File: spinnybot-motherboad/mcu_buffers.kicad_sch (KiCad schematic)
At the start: 13 parts, among them Q3 BC846, U2 XBP9B-DMWTB002, U5 ESP32-DEVKITC-32D, U7 SN74AHCT541DW

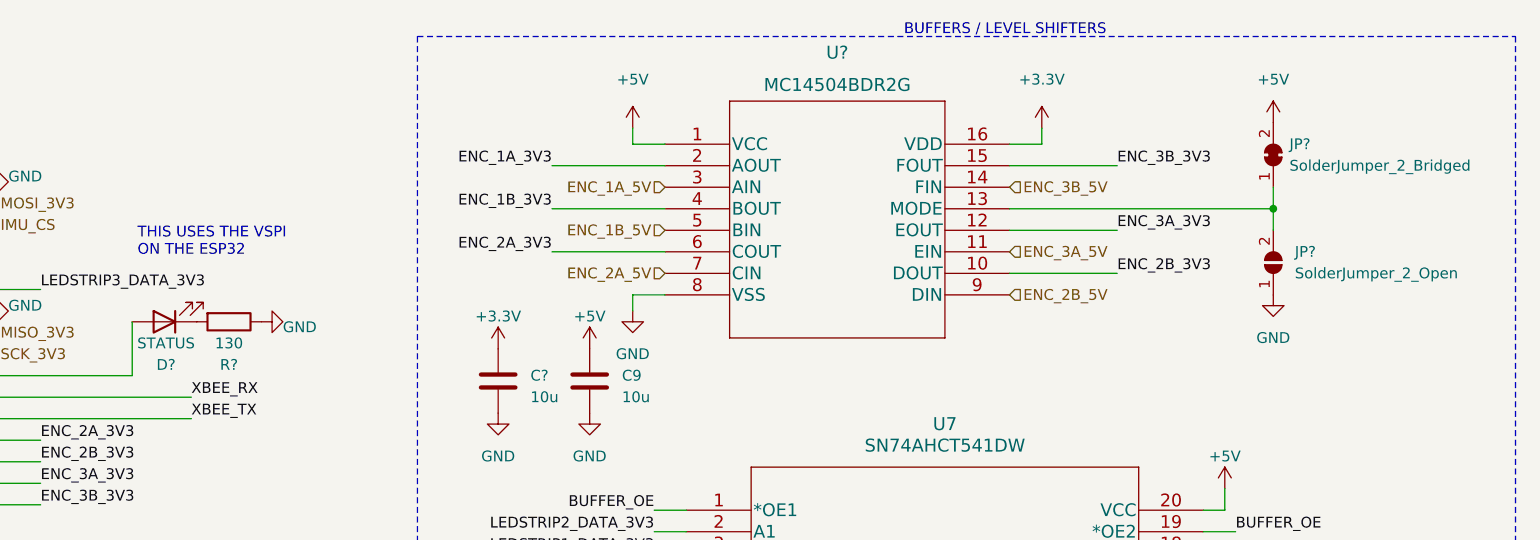
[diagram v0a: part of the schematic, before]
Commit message: Added 4 pin JST connector footprint and assigned footprints
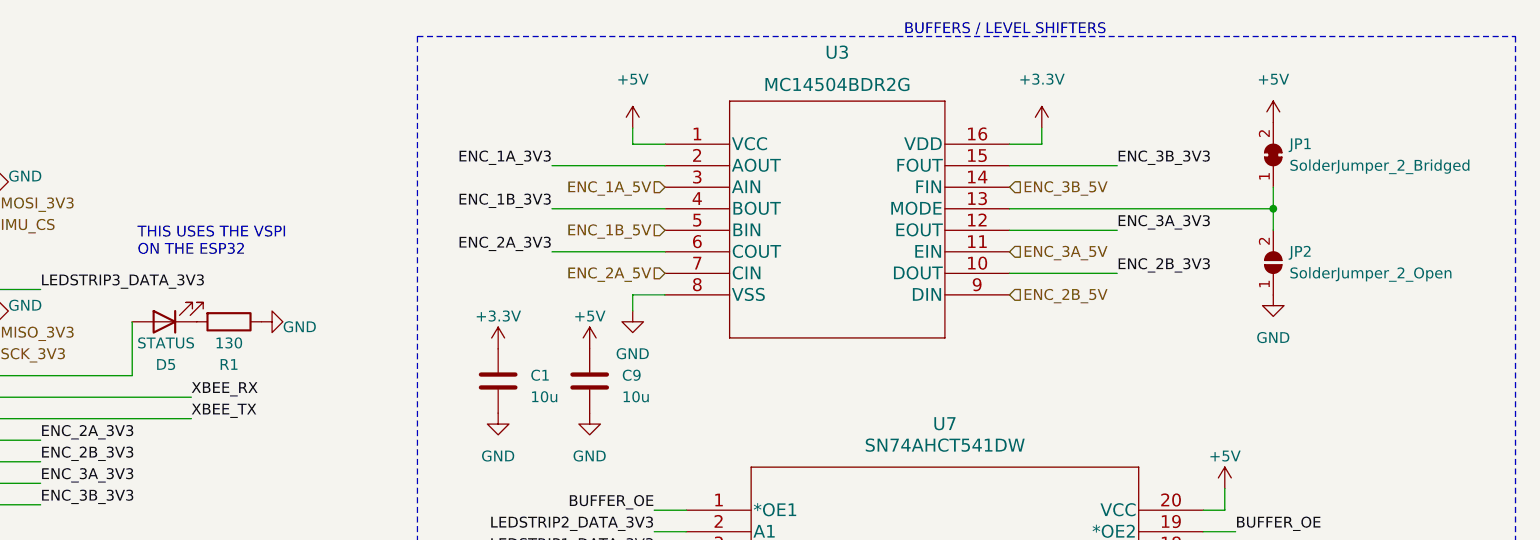
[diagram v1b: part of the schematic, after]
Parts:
- JP1: renamed from JP?; footprint (none) -> Jumper:SolderJumper-2_P1.3mm_Bridged_Pad1.0x1.5mm
- JP2: renamed from JP?; footprint (none) -> Jumper:SolderJumper-2_P1.3mm_Open_Pad1.0x1.5mm
- gave numbers to parts that had none: 4
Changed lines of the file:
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@@
   (symbol (lib_id "MC14504BDR2G:MC14504BDR2G") (at 181.61 30.48 0) (unit 1)
     (in_bom yes) (on_board yes) (fields_autoplaced)
-    (property "Reference" "U?" (id 0) (at 201.93 19.685 0)
+    (property "Reference" "U3" (id 0) (at 201.93 19.685 0)
       (effects (font (size 1.524 1.524)))
     )
@@
   (symbol (lib_id "Device:C") (at 161.925 58.42 0) (unit 1)
     (in_bom yes) (on_board yes) (fields_autoplaced)
-    (property "Reference" "C?" (id 0) (at 165.735 57.7849 0)
+    (property "Reference" "C1" (id 0) (at 165.735 57.7849 0)
       (effects (font (size 1.27 1.27)) (justify left))
     )
@@
   (symbol (lib_id "Jumper:SolderJumper_2_Bridged") (at 253.365 31.75 90) (unit 1)
     (in_bom yes) (on_board yes) (fields_autoplaced)
-    (property "Reference" "JP?" (id 0) (at 255.27 30.4799 90)
+    (property "Reference" "JP1" (id 0) (at 255.27 30.4799 90)
       (effects (font (size 1.27 1.27)) (justify right))
     )
@@
       (effects (font (size 1.27 1.27)) (justify right))
     )
-    (property "Footprint" "" (id 2) (at 253.365 31.75 0)
+    (property "Footprint" "Jumper:SolderJumper-2_P1.3mm_Bridged_Pad1.0x1.5mm" (id 2) (at 253.365 31.75 0)
       (effects (font (size 1.27 1.27)) hide)
     )
@@
   (symbol (lib_id "Device:R") (at 130.175 51.435 270) (unit 1)
     (in_bom yes) (on_board yes) (fields_autoplaced)
-    (property "Reference" "R?" (id 0) (at 130.175 56.515 90))
+    (property "Reference" "R1" (id 0) (at 130.175 56.515 90))
     (property "Value" "130" (id 1) (at 130.175 53.975 90))
     (property "Footprint" "Resistor_SMD:R_0805_2012Metric_Pad1.20x1.40mm_HandSolder" (id 2) (at 130.175 49.657 90)
@@
   (symbol (lib_id "Jumper:SolderJumper_2_Open") (at 253.365 44.45 90) (unit 1)
     (in_bom yes) (on_board yes) (fields_autoplaced)
-    (property "Reference" "JP?" (id 0) (at 255.905 43.1799 90)
-      (effects (font (size 1.27 1.27)) (justify right))
-    )
-    (property "Value" "SolderJumper_2_Open" (id 1) (at 255.905 45.7199 90)
-      (effects (font (size 1.27 1.27)) (justify right))
-    )
-    (property "Footprint" "" (id 2) (at 253.365 44.45 0)
+    (property "Reference" "JP2" (id 0) (at 255.27 43.1799 90)
+      (effects (font (size 1.27 1.27)) (justify right))
+    )
+    (property "Value" "SolderJumper_2_Open" (id 1) (at 255.27 45.7199 90)
+      (effects (font (size 1.27 1.27)) (justify right))
+    )
+    (property "Footprint" "Jumper:SolderJumper-2_P1.3mm_Open_Pad1.0x1.5mm" (id 2) (at 253.365 44.45 0)
       (effects (font (size 1.27 1.27)) hide)
     )
@@
   (symbol (lib_id "Device:LED") (at 122.555 51.435 180) (unit 1)
     (in_bom yes) (on_board yes) (fields_autoplaced)
-    (property "Reference" "D?" (id 0) (at 122.7455 56.515 0))
+    (property "Reference" "D5" (id 0) (at 122.7455 56.515 0))
     (property "Value" "STATUS" (id 1) (at 122.7455 53.975 0))
     (property "Footprint" "LED_SMD:LED_0805_2012Metric_Pad1.15x1.40mm_HandSolder" (id 2) (at 122.555 51.435 0)

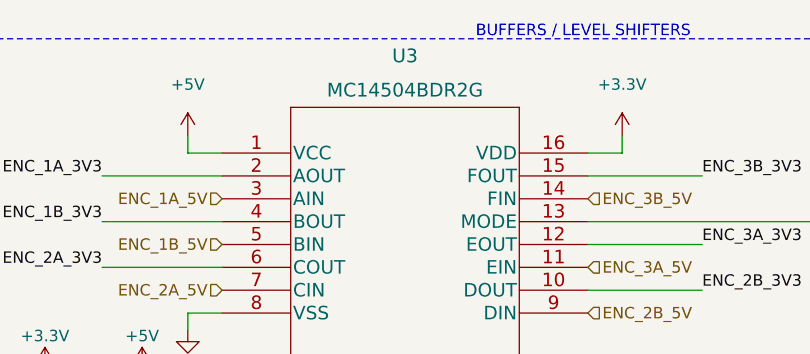
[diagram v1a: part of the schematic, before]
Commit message: Continued adding to board layout, added missing ESC connector footprint
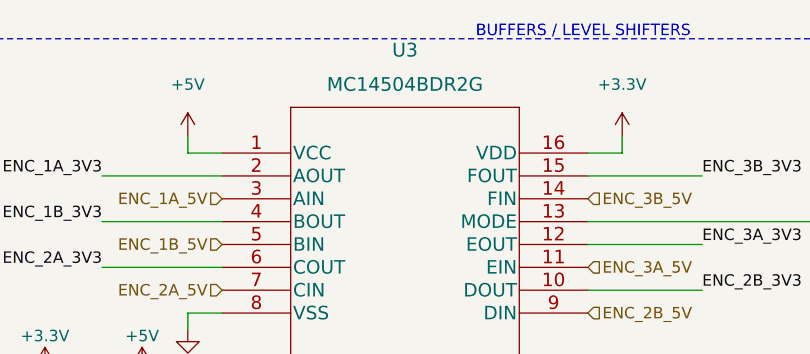
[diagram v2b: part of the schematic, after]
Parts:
- U3: footprint SOIC-16_ONS -> MC14504BDR2G:MC14504BDR2G
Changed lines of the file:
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@@
   (symbol (lib_id "MC14504BDR2G:MC14504BDR2G") (at 181.61 30.48 0) (unit 1)
     (in_bom yes) (on_board yes) (fields_autoplaced)
-    (property "Reference" "U3" (id 0) (at 201.93 19.685 0)
+    (property "Reference" "U3" (id 0) (at 201.93 19.05 0)
       (effects (font (size 1.524 1.524)))
     )
-    (property "Value" "MC14504BDR2G" (id 1) (at 201.93 23.495 0)
+    (property "Value" "MC14504BDR2G" (id 1) (at 201.93 22.86 0)
       (effects (font (size 1.524 1.524)))
     )
-    (property "Footprint" "SOIC-16_ONS" (id 2) (at 201.93 24.384 0)
+    (property "Footprint" "MC14504BDR2G:MC14504BDR2G" (id 2) (at 201.93 24.384 0)
       (effects (font (size 1.524 1.524)) hide)
     )

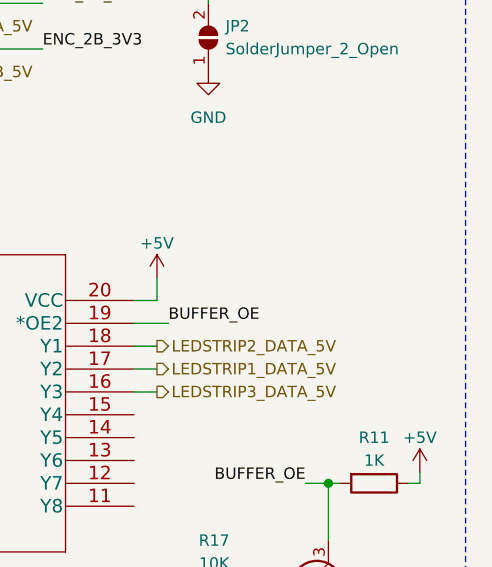
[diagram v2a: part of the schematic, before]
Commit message: Addressed Pratik's concerns about cap placement and missing caps
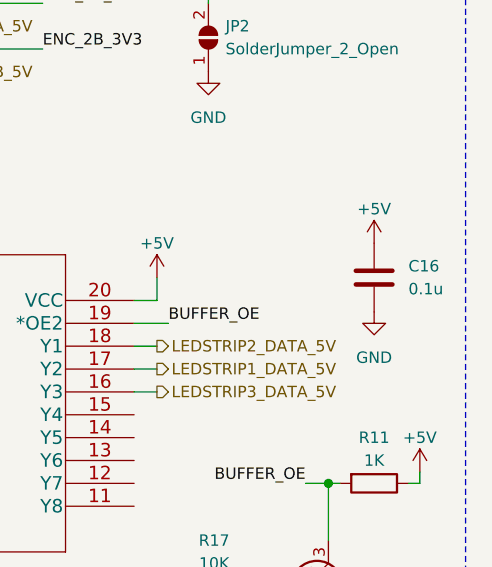
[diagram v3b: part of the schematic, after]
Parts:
- added C16: 0.1u, Capacitor_SMD:C_1206_3216Metric_Pad1.33x1.80mm_HandSolder, symbol Device:C
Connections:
- net +5V: now also C16.1
- net GND: now also C16.2
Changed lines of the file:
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@@
+    (pin "1")
+  )
+  (symbol (lib_id "power:+5V") (at 271.78 67.31 0) (unit 1)
+    (in_bom yes) (on_board yes) (fields_autoplaced)
+    (property "Reference" "#PWR0160" (id 0) (at 273.05 66.04 0)
+      (effects (font (size 1.27 1.27)) hide)
+    )
+    (property "Value" "+5V" (id 1) (at 271.78 63.5 0))
+    (property "Footprint" "" (id 2) (at 271.78 67.31 0)
+      (effects (font (size 1.27 1.27)) hide)
+    )
+    (property "Datasheet" "" (id 3) (at 271.78 67.31 0)
+      (effects (font (size 1.27 1.27)) hide)
+    )
     (pin "1")
   )
@@
     )
     (property "Datasheet" "" (id 3) (at 59.69 67.945 0)
+      (effects (font (size 1.27 1.27)) hide)
+    )
+    (pin "1")
+  )
+  (symbol (lib_id "power:GND") (at 271.78 74.93 0) (unit 1)
+    (in_bom yes) (on_board yes) (fields_autoplaced)
+    (property "Reference" "#PWR0161" (id 0) (at 273.05 73.66 0)
+      (effects (font (size 1.27 1.27)) hide)
+    )
+    (property "Value" "GND" (id 1) (at 271.78 80.01 0))
+    (property "Footprint" "" (id 2) (at 271.78 74.93 0)
+      (effects (font (size 1.27 1.27)) hide)
+    )
+    (property "Datasheet" "" (id 3) (at 271.78 74.93 0)
       (effects (font (size 1.27 1.27)) hide)
     )
@@
       (effects (font (size 1.27 1.27)) hide)
     )
+    (pin "1")
+    (pin "2")
+  )
+  (symbol (lib_id "Device:C") (at 271.78 71.12 0) (unit 1)
+    (in_bom yes) (on_board yes) (fields_autoplaced)
+    (property "Reference" "C16" (id 0) (at 275.59 69.8499 0)
+      (effects (font (size 1.27 1.27)) (justify left))
+    )
+    (property "Value" "0.1u" (id 1) (at 275.59 72.3899 0)
+      (effects (font (size 1.27 1.27)) (justify left))
+    )
+    (property "Footprint" "Capacitor_SMD:C_1206_3216Metric_Pad1.33x1.80mm_HandSolder" (id 2) (at 272.7452 74.93 0)
+      (effects (font (size 1.27 1.27)) hide)
+    )
+    (property "Datasheet" "~" (id 3) (at 271.78 71.12 0)
+      (effects (font (size 1.27 1.27)) hide)
+    )

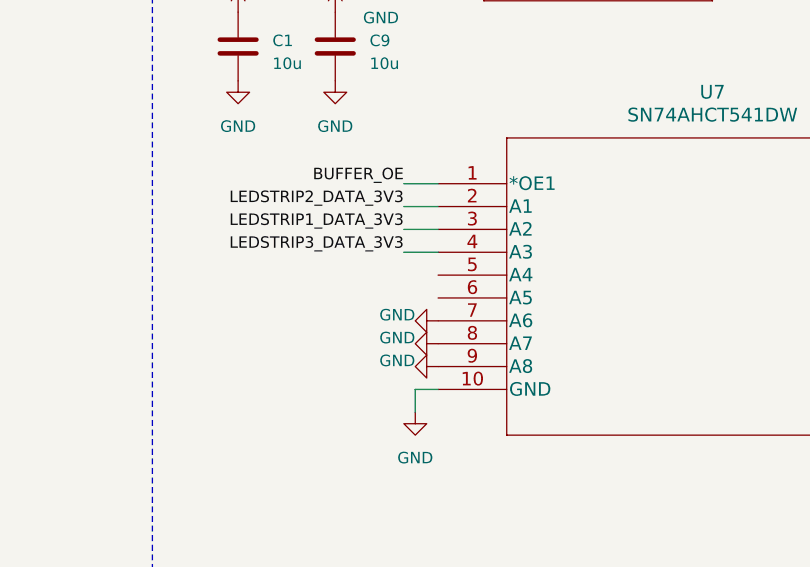
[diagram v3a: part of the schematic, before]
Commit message: tweaks to routing to make the ground plane more connected, add a top copper ground pour. move ESC FET.
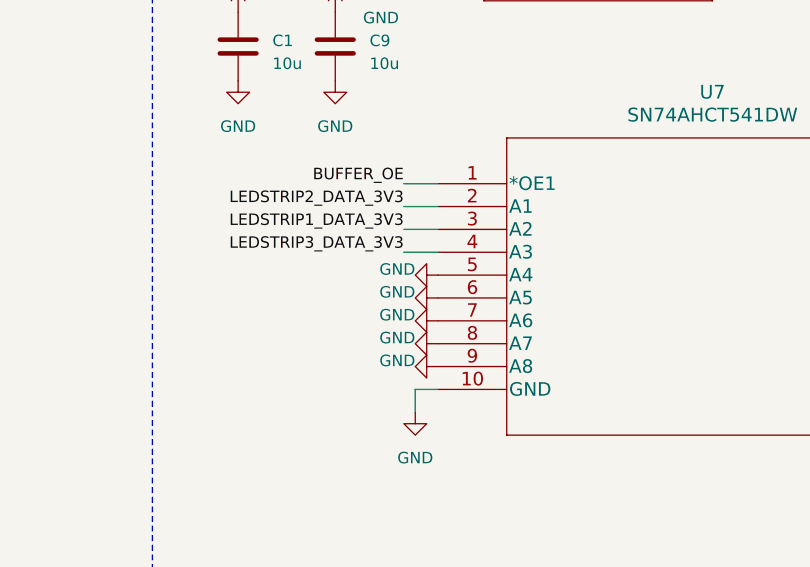
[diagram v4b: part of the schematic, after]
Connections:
- net GND: now also U7.5 (A4), U7.6 (A5)
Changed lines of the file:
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@@
+    (pin "1")
+  )
+  (symbol (lib_id "power:GND") (at 184.15 83.82 270) (unit 1)
+    (in_bom yes) (on_board yes)
+    (property "Reference" "#PWR0166" (id 0) (at 185.42 85.09 0)
+      (effects (font (size 1.27 1.27)) hide)
+    )
+    (property "Value" "GND" (id 1) (at 181.61 83.1849 90)
+      (effects (font (size 1.27 1.27)) (justify right))
+    )
+    (property "Footprint" "" (id 2) (at 184.15 83.82 0)
+      (effects (font (size 1.27 1.27)) hide)
+    )
+    (property "Datasheet" "" (id 3) (at 184.15 83.82 0)
+      (effects (font (size 1.27 1.27)) hide)
+    )
     (pin "1")
   )
@@
     (pin "2")
   )
+  (symbol (lib_id "power:GND") (at 184.15 86.36 270) (unit 1)
+    (in_bom yes) (on_board yes)
+    (property "Reference" "#PWR0167" (id 0) (at 185.42 87.63 0)
+      (effects (font (size 1.27 1.27)) hide)
+    )
+    (property "Value" "GND" (id 1) (at 181.61 85.7249 90)
+      (effects (font (size 1.27 1.27)) (justify right))
+    )
+    (property "Footprint" "" (id 2) (at 184.15 86.36 0)
+      (effects (font (size 1.27 1.27)) hide)
+    )
+    (property "Datasheet" "" (id 3) (at 184.15 86.36 0)
+      (effects (font (size 1.27 1.27)) hide)
+    )
+    (pin "1")
+  )
   (symbol (lib_id "power:GND") (at 59.69 67.945 270) (unit 1)
